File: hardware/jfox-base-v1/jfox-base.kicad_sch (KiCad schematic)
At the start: 0 parts

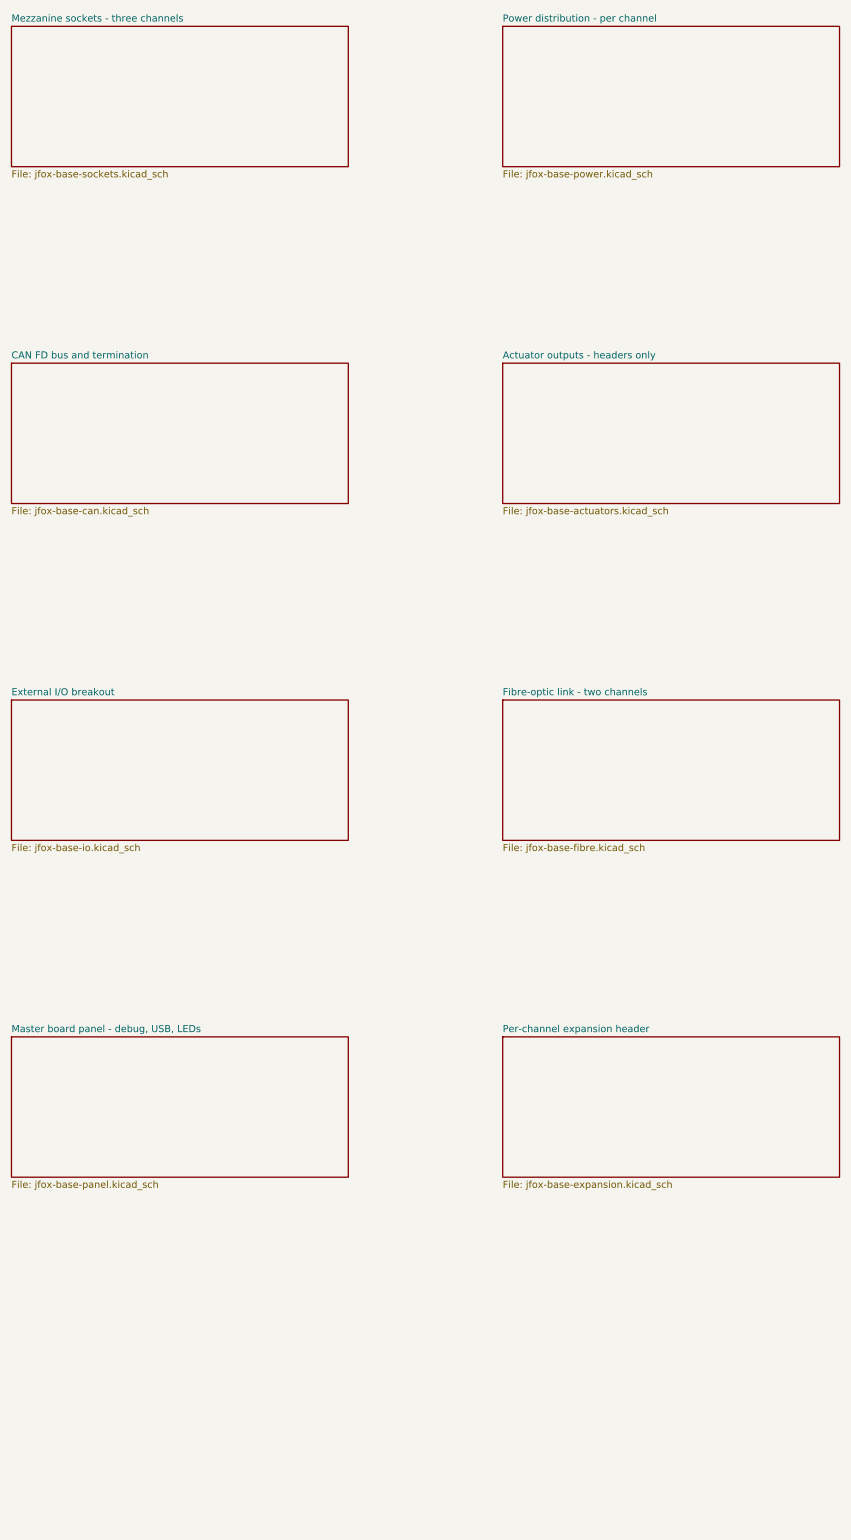
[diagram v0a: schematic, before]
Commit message: LTC4417 lands on the backplane, replacing the diode OR
It left the FCU when the power tree moved and never arrived here - the
backplane has been ORing its two airframe feeds with a pair of Schottkys,
which works and throws away the two things the part was chosen for:

  * Priority. A diode OR takes whichever feed is momentarily higher, so two
    supplies sitting 100 mV apart make the board chatter between them. The
    LTC4417 holds its selection until that source leaves its window.
  * A window. Under- and over-voltage per input, so a feed that has drifted
    out of spec is rejected rather than used because it is the higher of two
    bad ones.

It also drops ~0.4 V across a 5 V rail that the PMOS pass devices do not.

Two inputs, not three. V3 is tied to ground and its pass FET omitted, which
is how the datasheet says to leave an input out; inventing a third feed to
fill it would be worse. D50/D51 stay as reverse-polarity protection.

Three faults surfaced while wiring it, none of them the ORing:

  * The actuator headers still asked each channel for VDD_SERVO. That rail
    left the card's pinout when the power tree moved - servo power now runs
    from the backplane straight to the actuators and never passes through a
    card, which is the right way round. Three nets had nothing driving them.
  * EN was tied to +3V3, a rail the backplane does not have. It regulates
    nothing; the cards do. Now tied to the primary feed, so the part is
    enabled whenever there is power at all.
  * The expansion header overflowed. Its guard reported "25 spare signals
    will not fit a 20-pin header - widen it rather than dropping the
    overflow silently", which is exactly what it was written to catch. 2x15.

The far-face hole check earned itself again: a threshold divider placed on
the back landed under a card socket's through-holes. Bands on the back face
have to thread between sockets at y 20..27, 46..53 and 72..79.

  FCU        DRC 0 blocking, 105 parts, all checks pa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
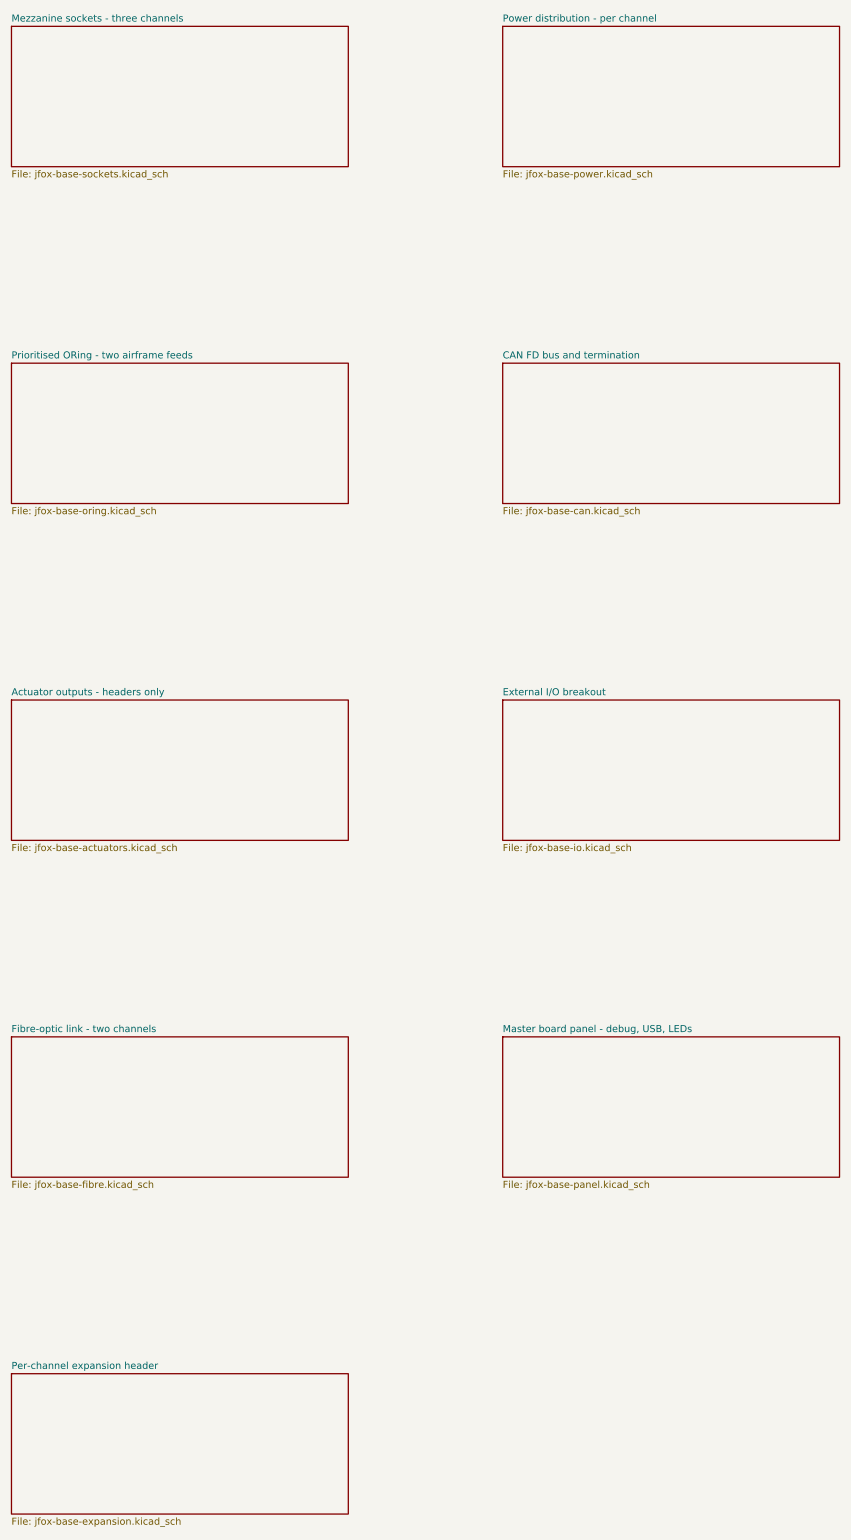
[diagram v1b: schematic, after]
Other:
- added sheet Prioritised ORing - two airframe feeds (jfox-base-oring.kicad_sch)
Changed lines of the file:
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@@
 		(instances
 			(project "jfox-base"
-				(path "/b2cc6ebd-b7ba-402a-ae78-fd348f9c718b"
+				(path "/06ecc874-cab5-4cc2-8ce6-7ea7d63700ec"
 					(page "2")
 				)
@@
 		(instances
 			(project "jfox-base"
-				(path "/b2cc6ebd-b7ba-402a-ae78-fd348f9c718b"
+				(path "/06ecc874-cab5-4cc2-8ce6-7ea7d63700ec"
 					(page "3")
 				)
@@
 		(stroke (width 0.1524)(type solid))
 		(fill (color 0 0 0 0.0000))
-		(property "Sheetname" "CAN FD bus and termination"
+		(property "Sheetname" "Prioritised ORing - two airframe feeds"
 			(at 25.4 100.89 0)
 			(effects (font (size 1.27 1.27))(justify left bottom))
 		)
-		(property "Sheetfile" "jfox-base-can.kicad_sch"
+		(property "Sheetfile" "jfox-base-oring.kicad_sch"
 			(at 25.4 127.6 0)
 			(effects (font (size 1.27 1.27))(justify left top))
@@
 		(instances
 			(project "jfox-base"
-				(path "/b2cc6ebd-b7ba-402a-ae78-fd348f9c718b"
+				(path "/06ecc874-cab5-4cc2-8ce6-7ea7d63700ec"
 					(page "4")
 				)
@@
 		(stroke (width 0.1524)(type solid))
 		(fill (color 0 0 0 0.0000))
-		(property "Sheetname" "Actuator outputs - headers only"
+		(property "Sheetname" "CAN FD bus and termination"
 			(at 114.30000000000001 100.89 0)
 			(effects (font (size 1.27 1.27))(justify left bottom))
 		)
-		(property "Sheetfile" "jfox-base-actuators.kicad_sch"
+		(property "Sheetfile" "jfox-base-can.kicad_sch"
 			(at 114.30000000000001 127.6 0)
 			(effects (font (size 1.27 1.27))(justify left top))
@@
 		(instances
 			(project "jfox-base"
-				(path "/b2cc6ebd-b7ba-402a-ae78-fd348f9c718b"
+				(path "/06ecc874-cab5-4cc2-8ce6-7ea7d63700ec"
 					(page "5")
 				)
@@
 		(stroke (width 0.1524)(type solid))
 		(fill (color 0 0 0 0.0000))
-		(property "Sheetname" "External I/O breakout"
+		(property "Sheetname" "Actuator outputs - headers only"
 			(at 25.4 161.85 0)
 			(effects (font (size 1.27 1.27))(justify left bottom))
 		)
-		(property "Sheetfile" "jfox-base-io.kicad_sch"
+		(property "Sheetfile" "jfox-base-actuators.kicad_sch"
 			(at 25.4 188.56 0)
 			(effects (font (size 1.27 1.27))(justify left top))
@@
 		(instances
 			(project "jfox-base"
-				(path "/b2cc6ebd-b7ba-402a-ae78-fd348f9c718b"
+				(path "/06ecc874-cab5-4cc2-8ce6-7ea7d63700ec"
 					(page "6")
 				)
@@
 		(stroke (width 0.1524)(type solid))
 		(fill (color 0 0 0 0.0000))
-		(property "Sheetname" "Fibre-optic link - two channels"
+		(property "Sheetname" "External I/O breakout"
 			(at 114.30000000000001 161.85 0)
 			(effects (font (size 1.27 1.27))(justify left bottom))
 		)
-		(property "Sheetfile" "jfox-base-fibre.kicad_sch"
+		(property "Sheetfile" "jfox-base-io.kicad_sch"
 			(at 114.30000000000001 188.56 0)
 			(effects (font (size 1.27 1.27))(justify left top))
@@
 		(instances
 			(project "jfox-base"
-				(path "/b2cc6ebd-b7ba-402a-ae78-fd348f9c718b"
+				(path "/06ecc874-cab5-4cc2-8ce6-7ea7d63700ec"
 					(page "7")
 				)
@@
 		(stroke (width 0.1524)(type solid))
 		(fill (color 0 0 0 0.0000))
-		(property "Sheetname" "Master board panel - debug, USB, LEDs"
+		(property "Sheetname" "Fibre-optic link - two channels"
 			(at 25.4 222.81 0)
 			(effects (font (size 1.27 1.27))(justify left bottom))
 		)
-		(property "Sheetfile" "jfox-base-panel.kicad_sch"
+		(property "Sheetfile" "jfox-base-fibre.kicad_sch"
 			(at 25.4 249.52 0)
 			(effects (font (size 1.27 1.27))(justify left top))
@@
 		(instances
 			(project "jfox-base"
-				(path "/b2cc6ebd-b7ba-402a-ae78-fd348f9c718b"
+				(path "/06ecc874-cab5-4cc2-8ce6-7ea7d63700ec"
 					(page "8")
 				)
@@
 		(stroke (width 0.1524)(type solid))
 		(fill (color 0 0 0 0.0000))
-		(property "Sheetname" "Per-channel expansion header"
+		(property "Sheetname" "Master board panel - debug, USB, LEDs"
 			(at 114.30000000000001 222.81 0)
 			(effects (font (size 1.27 1.27))(justify left bottom))
 		)
-		(property "Sheetfile" "jfox-base-expansion.kicad_sch"
+		(property "Sheetfile" "jfox-base-panel.kicad_sch"
 			(at 114.30000000000001 249.52 0)
 			(effects (font (size 1.27 1.27))(justify left top))
@@
 		(instances
 			(project "jfox-base"
-				(path "/b2cc6ebd-b7ba-402a-ae78-fd348f9c718b"
+				(path "/06ecc874-cab5-4cc2-8ce6-7ea7d63700ec"
 					(page "9")
 				)
 			)
+		)
+	)
+	(sheet
+		(at 25.4 284.48)
+		(size 60.96 25.4)
+		(fields_autoplaced yes)
+		(stroke (width 0.1524)(type solid))
+		(fill (color 0 0 0 0.0000))
+		(property "Sheetname" "Per-channel expansion header"
+			(at 25.4 283.77 0)
+			(effects (font (size 1.27 1.27))(justify left bottom))
+		)
+		(property "Sheetfile" "jfox-base-expansion.kicad_sch"
+			(at 25.4 310.48 0)
+			(effects (font (size 1.27 1.27))(justify left top))
+		)
+		(instances
+			(project "jfox-base"
+				(path "/06ecc874-cab5-4cc2-8ce6-7ea7d63700ec"
+					(page "10")
+				)
+			)
